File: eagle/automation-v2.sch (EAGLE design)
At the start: 96 parts, among them IC1 MEGA48/88/168-AU, IC2 DS2482-100S, IC3 DS2482-100S, IC4 78L33, K1 SRD-05VDC-SL-C, K2 SRD-05VDC-SL-C, K3 SRD-05VDC-SL-C, K4 SRD-05VDC-SL-C, Q1 BSS123, Q2 BSS123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

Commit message: Initial PCB trace
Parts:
- added C19, C20, C21: (no value), rcl:CPOL-EUE5-10.5
- added R37, R38, R39: (no value), rcl:R-EU_M1206
- JP2, JP3: device pinhead:PINHD-1X2/90 -> pinhead:PINHD-1X2
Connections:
- new net N$14: C19.+, K31.2, R37.2
- new net N$63: C20.+, K21.2, R38.1
- new net N$66: C21.+, K11.2, R39.1
- net 12V: now also R37.1, R38.2, R39.2; no longer K11.2, K21.2, K31.2
- net GND: now also C19.-, C20.-, C21.-
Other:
- moved on the sheet: D1, D2, D3, LED1, LED2, LED3, LED4, R15, R17, R20

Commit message: updated PCB trace
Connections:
- net N$23: now also IC1.PB2(SS/OC1B/PCINT2); no longer IC1.PD7(AIN1/PCINT23)
- net N$24: now also IC1.PB1(OC1A/PCINT1); no longer IC1.PB0(ICP1/CLKO/PCINT0)
- net N$46: now also IC1.PD7(AIN1/PCINT23); no longer IC1.PB1(OC1A/PCINT1)
- net N$53: now also IC1.PB0(ICP1/CLKO/PCINT0); no longer IC1.PB2(SS/OC1B/PCINT2)
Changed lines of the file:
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@@
 <clearance class="0" value="0.254"/>
 </class>
-<class number="1" name="POWER" width="0.4064" drill="0">
+<class number="1" name="POWER" width="0.508" drill="0">
 <clearance class="1" value="0.254"/>
 </class>
@@
 <pinref part="R15" gate="G$1" pin="1"/>
 <wire x1="-27.94" y1="-53.34" x2="-22.86" y2="-53.34" width="0.1524" layer="91"/>
-<pinref part="IC1" gate="1" pin="PD7(AIN1/PCINT23)"/>
-<wire x1="-43.18" y1="35.56" x2="-33.02" y2="35.56" width="0.1524" layer="91"/>
-<wire x1="-33.02" y1="35.56" x2="-33.02" y2="-45.72" width="0.1524" layer="91"/>
+<wire x1="-33.02" y1="25.4" x2="-33.02" y2="-45.72" width="0.1524" layer="91"/>
 <wire x1="-27.94" y1="-45.72" x2="-33.02" y2="-45.72" width="0.1524" layer="91"/>
 <junction x="-27.94" y="-45.72"/>
+<pinref part="IC1" gate="1" pin="PB2(SS/OC1B/PCINT2)"/>
+<wire x1="-43.18" y1="25.4" x2="-33.02" y2="25.4" width="0.1524" layer="91"/>
 </segment>
 </net>
@@
 <pinref part="R17" gate="G$1" pin="1"/>
 <wire x1="-27.94" y1="-86.36" x2="-22.86" y2="-86.36" width="0.1524" layer="91"/>
-<pinref part="IC1" gate="1" pin="PB0(ICP1/CLKO/PCINT0)"/>
-<wire x1="-43.18" y1="30.48" x2="-35.56" y2="30.48" width="0.1524" layer="91"/>
 <wire x1="-27.94" y1="-78.74" x2="-35.56" y2="-78.74" width="0.1524" layer="91"/>
-<wire x1="-35.56" y1="-78.74" x2="-35.56" y2="30.48" width="0.1524" layer="91"/>
+<wire x1="-35.56" y1="-78.74" x2="-35.56" y2="27.94" width="0.1524" layer="91"/>
 <junction x="-27.94" y="-78.74"/>
+<pinref part="IC1" gate="1" pin="PB1(OC1A/PCINT1)"/>
+<wire x1="-43.18" y1="27.94" x2="-35.56" y2="27.94" width="0.1524" layer="91"/>
 </segment>
 </net>
@@
 <pinref part="R20" gate="G$1" pin="1"/>
 <wire x1="-45.72" y1="-86.36" x2="-50.8" y2="-86.36" width="0.1524" layer="91"/>
-<pinref part="IC1" gate="1" pin="PB1(OC1A/PCINT1)"/>
-<wire x1="-43.18" y1="27.94" x2="-38.1" y2="27.94" width="0.1524" layer="91"/>
 <wire x1="-45.72" y1="-78.74" x2="-38.1" y2="-78.74" width="0.1524" layer="91"/>
-<wire x1="-38.1" y1="-78.74" x2="-38.1" y2="27.94" width="0.1524" layer="91"/>
+<wire x1="-38.1" y1="-78.74" x2="-38.1" y2="35.56" width="0.1524" layer="91"/>
 <junction x="-45.72" y="-78.74"/>
+<pinref part="IC1" gate="1" pin="PD7(AIN1/PCINT23)"/>
+<wire x1="-38.1" y1="35.56" x2="-43.18" y2="35.56" width="0.1524" layer="91"/>
 </segment>
 </net>
@@
 <pinref part="R26" gate="G$1" pin="1"/>
 <wire x1="-45.72" y1="-53.34" x2="-50.8" y2="-53.34" width="0.1524" layer="91"/>
-<pinref part="IC1" gate="1" pin="PB2(SS/OC1B/PCINT2)"/>
-<wire x1="-43.18" y1="25.4" x2="-40.64" y2="25.4" width="0.1524" layer="91"/>
 <wire x1="-45.72" y1="-45.72" x2="-40.64" y2="-45.72" width="0.1524" layer="91"/>
-<wire x1="-40.64" y1="-45.72" x2="-40.64" y2="25.4" width="0.1524" layer="91"/>
+<wire x1="-40.64" y1="-45.72" x2="-40.64" y2="30.48" width="0.1524" layer="91"/>
 <junction x="-45.72" y="-45.72"/>
-</segment>
-</net>
+<pinref part="IC1" gate="1" pin="PB0(ICP1/CLKO/PCINT0)"/>
+<wire x1="-40.64" y1="30.48" x2="-43.18" y2="30.48" width="0.1524" layer="91"/>
+</segment>
+</net>

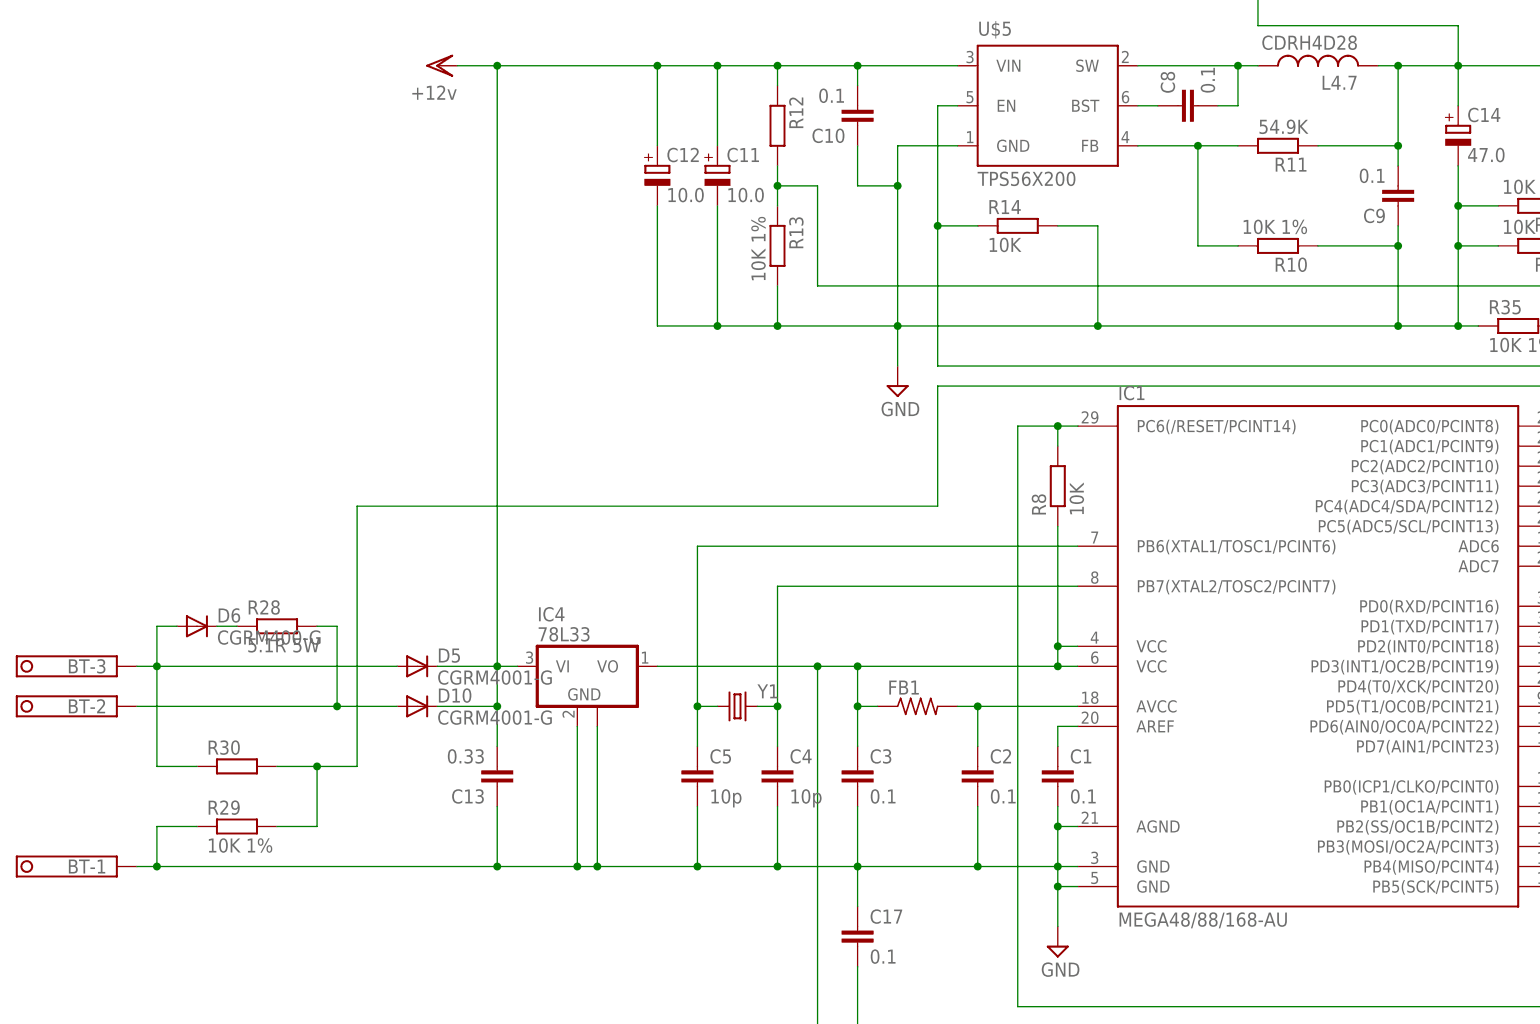
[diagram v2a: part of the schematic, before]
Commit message: RC version of PCB trace
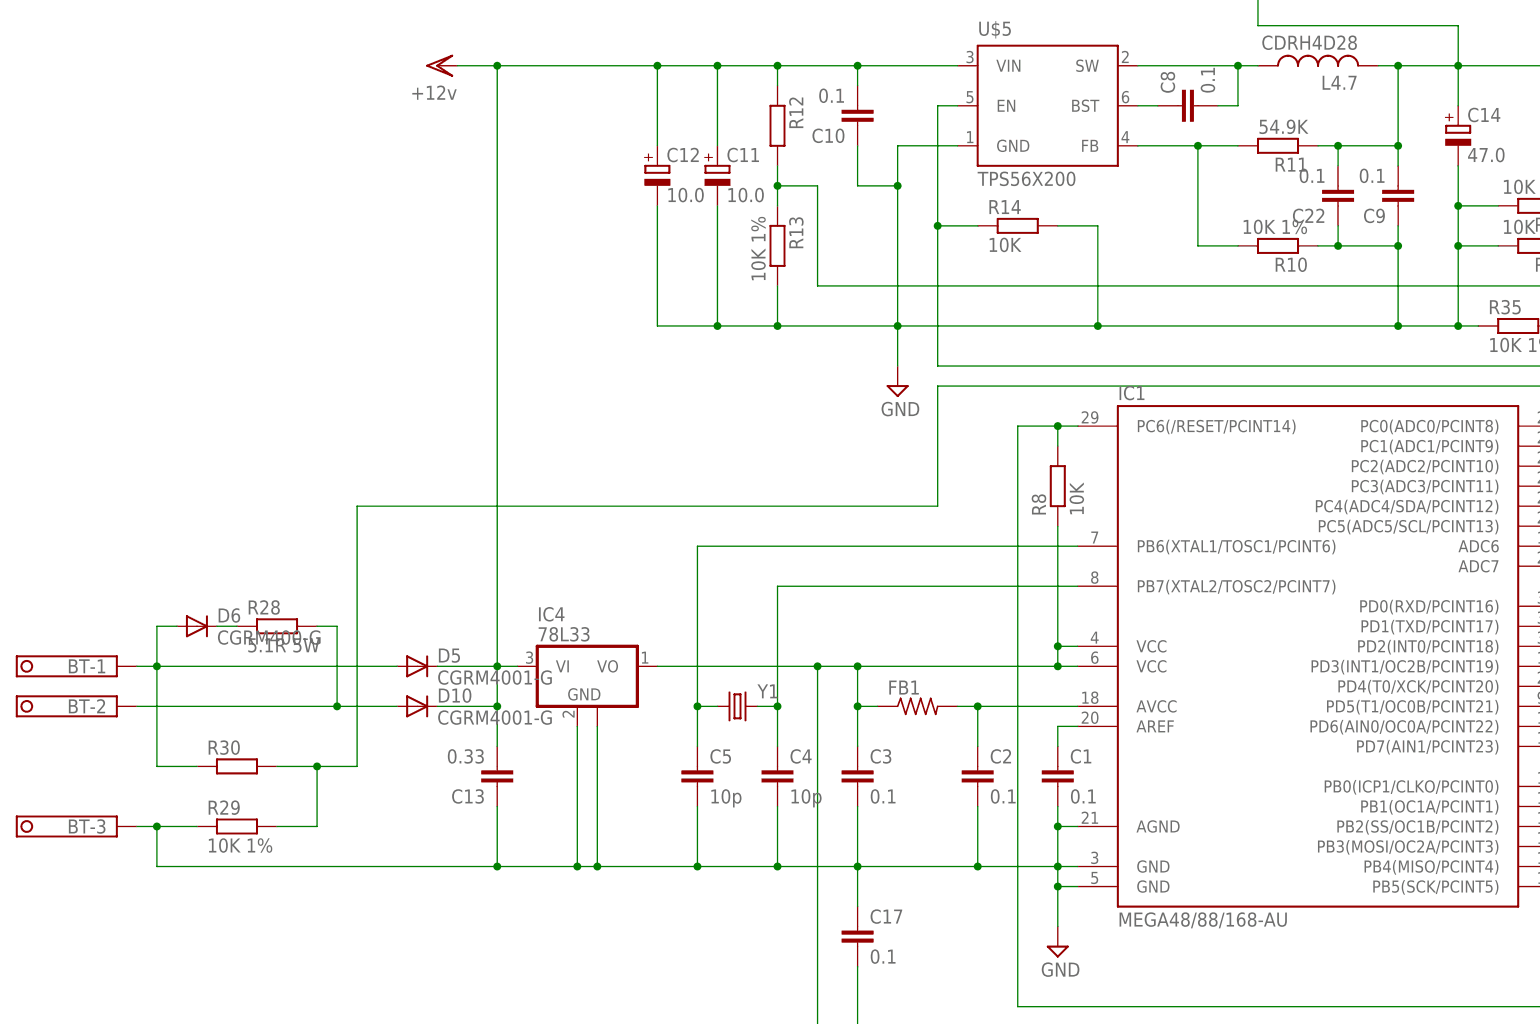
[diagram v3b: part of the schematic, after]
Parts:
- added C22: 0.1, rcl:C-EUC0805
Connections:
- net GND: now also BT-3.K, C22.1; no longer BT-1.K
- net N$12: now also BT-1.K; no longer BT-3.K
- net Z5V: now also C22.2
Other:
- moved on the sheet: BT-1, BT-3
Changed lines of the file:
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@@
 <part name="R39" library="rcl" deviceset="R-EU_" device="M1206"/>
 <part name="C21" library="rcl" deviceset="CPOL-EU" device="E5-10.5"/>
+<part name="C22" library="rcl" deviceset="C-EU" device="C0805" value="0.1"/>
 </parts>
 <sheets>
@@
 <instance part="V4" gate="G$1" x="-109.22" y="-58.42" rot="MR270"/>
 <instance part="D5" gate="G$1" x="-187.96" y="45.72"/>
-<instance part="BT" gate="-1" x="-226.06" y="20.32" rot="R180"/>
+<instance part="BT" gate="-1" x="-226.06" y="45.72" rot="R180"/>
 <instance part="BT" gate="-2" x="-226.06" y="40.64" rot="R180"/>
-<instance part="BT" gate="-3" x="-226.06" y="45.72" rot="R180"/>
+<instance part="BT" gate="-3" x="-226.06" y="25.4" rot="R180"/>
 <instance part="D6" gate="G$1" x="-215.9" y="50.8"/>
 <instance part="R28" gate="G$1" x="-205.74" y="50.8"/>
@@
 <instance part="R39" gate="G$1" x="22.86" y="-86.36"/>
 <instance part="C21" gate="G$1" x="2.54" y="-86.36" rot="MR90"/>
+<instance part="C22" gate="G$1" x="-71.12" y="104.14" rot="R180"/>
 </instances>
 <busses>
@@
 <junction x="-167.64" y="20.32"/>
 <wire x1="-177.8" y1="20.32" x2="-220.98" y2="20.32" width="0.1524" layer="91"/>
-<pinref part="BT" gate="-1" pin="K"/>
 <junction x="-177.8" y="20.32"/>
 <pinref part="R29" gate="G$1" pin="1"/>
-<wire x1="-220.98" y1="20.32" x2="-223.52" y2="20.32" width="0.1524" layer="91"/>
 <wire x1="-215.9" y1="25.4" x2="-220.98" y2="25.4" width="0.1524" layer="91"/>
 <wire x1="-220.98" y1="25.4" x2="-220.98" y2="20.32" width="0.1524" layer="91"/>
-<junction x="-220.98" y="20.32"/>
 <pinref part="C17" gate="G$1" pin="1"/>
 <wire x1="-132.08" y1="15.24" x2="-132.08" y2="20.32" width="0.1524" layer="91"/>
+<pinref part="BT" gate="-3" pin="K"/>
+<wire x1="-223.52" y1="25.4" x2="-220.98" y2="25.4" width="0.1524" layer="91"/>
+<junction x="-220.98" y="25.4"/>
 </segment>
 <segment>
@@
 <wire x1="-63.5" y1="88.9" x2="-55.88" y2="88.9" width="0.1524" layer="91"/>
 <wire x1="-63.5" y1="101.6" x2="-63.5" y2="99.06" width="0.1524" layer="91"/>
-<wire x1="-63.5" y1="99.06" x2="-73.66" y2="99.06" width="0.1524" layer="91"/>
+<wire x1="-63.5" y1="99.06" x2="-71.12" y2="99.06" width="0.1524" layer="91"/>
 <pinref part="R10" gate="G$1" pin="1"/>
+<wire x1="-71.12" y1="99.06" x2="-73.66" y2="99.06" width="0.1524" layer="91"/>
 <wire x1="-63.5" y1="99.06" x2="-63.5" y2="88.9" width="0.1524" layer="91"/>
 <junction x="-63.5" y="99.06"/>
 <junction x="-63.5" y="88.9"/>
+<pinref part="C22" gate="G$1" pin="1"/>
+<wire x1="-71.12" y1="101.6" x2="-71.12" y2="99.06" width="0.1524" layer="91"/>
+<junction x="-71.12" y="99.06"/>
 </segment>
 <segment>
@@
 </segment>
 </net>
-<net name="N$3" class="0">
+<net name="N$3" class="1">
 <segment>
 <pinref part="U$5" gate="G$1" pin="SW"/>
@@
 <pinref part="R11" gate="G$1" pin="1"/>
 <wire x1="-63.5" y1="111.76" x2="-63.5" y2="109.22" width="0.1524" layer="91"/>
-<wire x1="-73.66" y1="111.76" x2="-63.5" y2="111.76" width="0.1524" layer="91"/>
+<wire x1="-73.66" y1="111.76" x2="-71.12" y2="111.76" width="0.1524" layer="91"/>
 <junction x="-63.5" y="111.76"/>
+<wire x1="-71.12" y1="111.76" x2="-63.5" y2="111.76" width="0.1524" layer="91"/>
 <wire x1="-25.4" y1="91.44" x2="-25.4" y2="121.92" width="0.1524" layer="91"/>
 <wire x1="-25.4" y1="121.92" x2="-55.88" y2="121.92" width="0.1524" layer="91"/>
@@
 <junction x="-73.66" y="149.86"/>
 <junction x="12.7" y="81.28"/>
+<pinref part="C22" gate="G$1" pin="2"/>
+<wire x1="-71.12" y1="109.22" x2="-71.12" y2="111.76" width="0.1524" layer="91"/>
+<junction x="-71.12" y="111.76"/>
 </segment>
 </net>
@@
 <net name="N$12" class="1">
 <segment>
-<pinref part="BT" gate="-3" pin="K"/>
 <pinref part="D5" gate="G$1" pin="A"/>
-<wire x1="-223.52" y1="45.72" x2="-220.98" y2="45.72" width="0.1524" layer="91"/>
 <pinref part="D6" gate="G$1" pin="A"/>
 <wire x1="-220.98" y1="45.72" x2="-190.5" y2="45.72" width="0.1524" layer="91"/>
@@
 <wire x1="-215.9" y1="33.02" x2="-220.98" y2="33.02" width="0.1524" layer="91"/>
 <wire x1="-220.98" y1="33.02" x2="-220.98" y2="45.72" width="0.1524" layer="91"/>
-</segment>
-</net>
+<pinref part="BT" gate="-1" pin="K"/>
+<wire x1="-223.52" y1="45.72" x2="-220.98" y2="45.72" width="0.1524" layer="91"/>
+</segment>
+</net>
